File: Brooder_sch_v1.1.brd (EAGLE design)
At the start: 90 x 75 mm, 30 parts, among them J1 DCJ0202, J2 1X2-3.5MM, J3 DCJ0202, J4 1X2-3.5MM, U1 328P

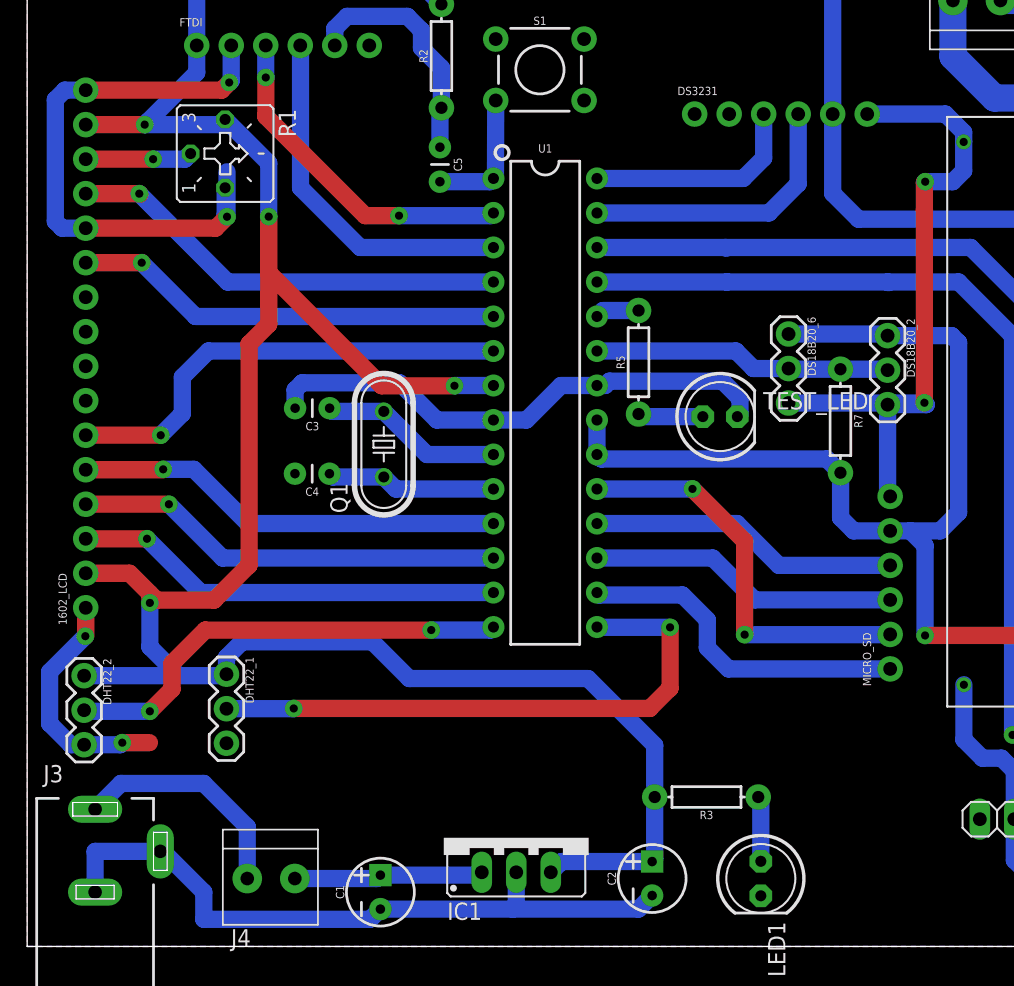
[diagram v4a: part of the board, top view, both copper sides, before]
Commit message: Links lcd and dht grounds
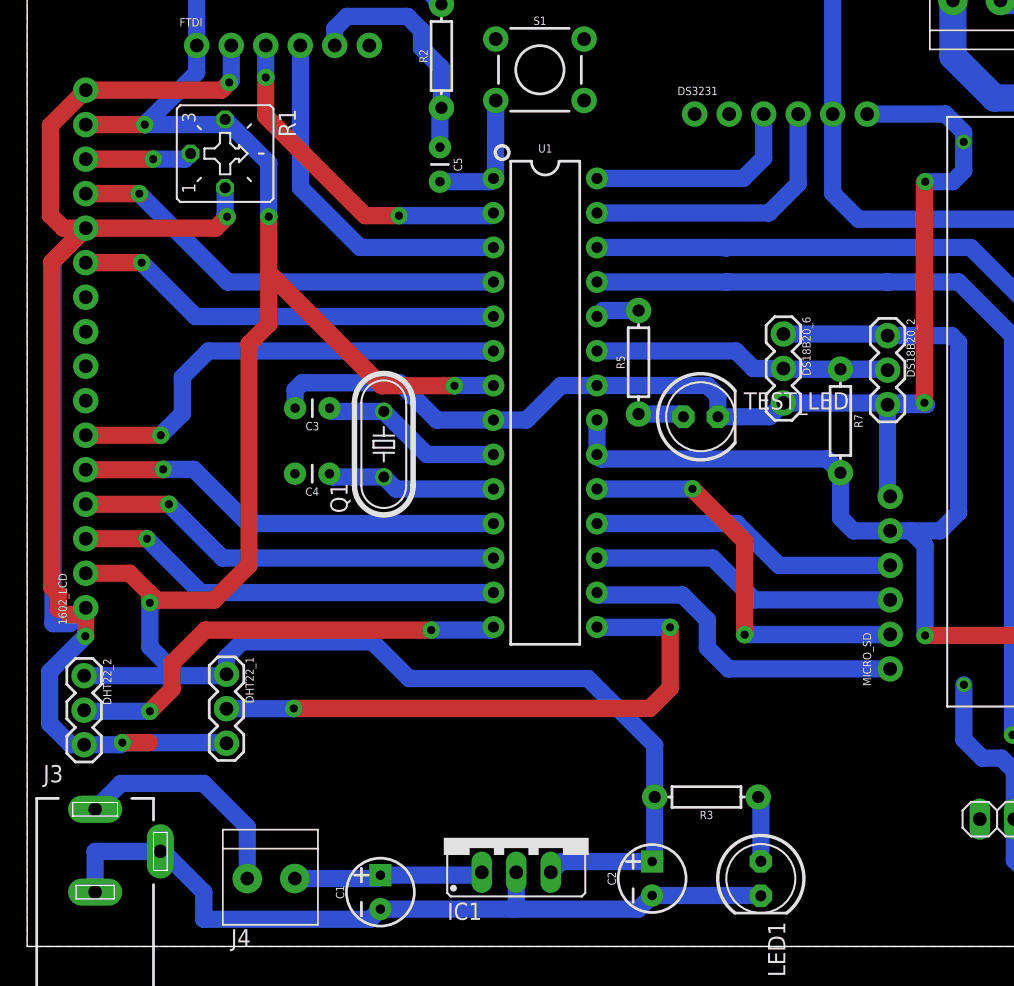
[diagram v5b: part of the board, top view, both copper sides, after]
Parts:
- moved TEST_LED 1.43 mm to (49.6, 39.0)
- moved DS18B20_6 0.38 mm to (55.7, 45.1)
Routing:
- net GND: track 236.1 -> 315.9 mm
- net N$1: track 4.81 -> 3.38 mm
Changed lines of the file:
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@@
 <attribute name="PROD_ID" value="XXX-00000" x="63.33" y="44.96" size="1.778" layer="27" rot="R270" display="off"/>
 </element>
-<element name="DS18B20_6" library="SparkFun-Connectors" package="1X03" value="455-1750-1-ND" x="56.04" y="45.08" rot="R270">
-<attribute name="PROD_ID" value="XXX-00000" x="56.04" y="45.08" size="1.778" layer="27" rot="R270" display="off"/>
+<element name="DS18B20_6" library="SparkFun-Connectors" package="1X03" value="455-1750-1-ND" x="55.66" y="45.08" rot="R270">
+<attribute name="PROD_ID" value="XXX-00000" x="55.66" y="45.08" size="1.778" layer="27" rot="R270" display="off"/>
 </element>
 <element name="FTDI" library="SparkFun-Connectors" package="1X06_NO_SILK" value="" x="12.48" y="66.32">
@@
 <attribute name="PROD_ID" value="RES-09327" x="45" y="43" size="1.778" layer="27" rot="R90" display="off"/>
 </element>
-<element name="TEST_LED" library="adafruit" package="LED5MM" value="" x="51" y="39"/>
+<element name="TEST_LED" library="adafruit" package="LED5MM" value="" x="49.57" y="38.99"/>
 <element name="DS3231" library="SparkFun-Connectors" package="1X06_NO_SILK" value="" x="49.13" y="61.27">
 <attribute name="PROD_ID" value="CONN-08437" x="49.13" y="61.27" size="1.778" layer="27" display="off"/>
@@
 <wire x1="13.87" y1="52.87" x2="14.71" y2="53.71" width="1.27" layer="1"/>
 <via x="14.71" y="53.71" extent="1-16" drill="0.6" diameter="1.3"/>
-<wire x1="14.71" y1="53.71" x2="14.71" y2="57.02" width="1.27" layer="16"/>
-<wire x1="52.47" y1="40.32" x2="52.47" y2="39.2" width="1.27" layer="16"/>
-<wire x1="52.47" y1="39.2" x2="52.27" y2="39" width="1.27" layer="16"/>
 <wire x1="41.94" y1="41.29" x2="42.54" y2="41.29" width="1.27" layer="16"/>
-<wire x1="42.54" y1="41.29" x2="42.86" y2="41.61" width="1.27" layer="16"/>
-<wire x1="42.86" y1="41.61" x2="51.18" y2="41.61" width="1.27" layer="16"/>
-<wire x1="51.18" y1="41.61" x2="52.47" y2="40.32" width="1.27" layer="16"/>
 <contactref element="U$2" pad="IN(-VE)"/>
 <contactref element="U$2" pad="OUT(-VE)"/>
@@
 <via x="66.04" y="40.02" extent="1-16" drill="0.6" diameter="1.3"/>
 <wire x1="66.04" y1="40.02" x2="66.02" y2="40" width="1.27" layer="16"/>
-<wire x1="66.02" y1="40" x2="56.04" y2="40" width="1.27" layer="16"/>
+<wire x1="66.02" y1="40" x2="55.66" y2="40" width="1.27" layer="16"/>
 <wire x1="66.04" y1="40.02" x2="66.18" y2="39.88" width="1.27" layer="16"/>
 <wire x1="66.18" y1="39.88" x2="63.33" y2="39.88" width="1.27" layer="16"/>
@@
 <wire x1="39.29" y1="41.29" x2="41.94" y2="41.29" width="1.27" layer="16"/>
 <wire x1="36.75" y1="38.75" x2="39.29" y2="41.29" width="1.27" layer="16"/>
-<wire x1="4.31" y1="52.87" x2="2.57" y2="52.87" width="1.27" layer="16"/>
-<wire x1="2.57" y1="52.87" x2="2.07" y2="53.37" width="1.27" layer="16"/>
-<wire x1="2.07" y1="53.37" x2="2.07" y2="62.33" width="1.27" layer="16"/>
-<wire x1="2.77" y1="63.03" x2="4.31" y2="63.03" width="1.27" layer="16"/>
-<wire x1="2.07" y1="62.33" x2="2.77" y2="63.03" width="1.27" layer="16"/>
 <wire x1="85.57" y1="67.95" x2="85.57" y2="69.75" width="2" layer="16"/>
 <wire x1="85.57" y1="69.75" x2="82.57" y2="72.75" width="2" layer="16"/>
@@
 <wire x1="14.57" y1="55.8454" x2="14.57" y2="53.85" width="1.27" layer="16"/>
 <wire x1="14.57" y1="53.85" x2="14.71" y2="53.71" width="1.27" layer="16"/>
+<wire x1="7" y1="15" x2="14.63" y2="15" width="1.27" layer="16"/>
+<wire x1="14.63" y1="15" x2="14.67" y2="14.96" width="1.27" layer="16"/>
+<wire x1="4.31" y1="52.87" x2="1.9" y2="50.46" width="1.27" layer="16"/>
+<wire x1="1.9" y1="50.46" x2="1.9" y2="23.76" width="1.27" layer="16"/>
+<wire x1="1.9" y1="23.76" x2="3.14" y2="23.76" width="1.27" layer="16"/>
+<wire x1="3.14" y1="23.76" x2="4.31" y2="24.93" width="1.27" layer="16"/>
+<wire x1="4.31" y1="63.03" x2="1.71" y2="60.43" width="1.27" layer="1"/>
+<wire x1="2.66" y1="52.87" x2="4.31" y2="52.87" width="1.27" layer="1"/>
+<wire x1="1.71" y1="60.43" x2="1.71" y2="53.82" width="1.27" layer="1"/>
+<wire x1="1.71" y1="53.82" x2="2.66" y2="52.87" width="1.27" layer="1"/>
+<wire x1="4.31" y1="52.87" x2="1.81" y2="50.37" width="1.27" layer="1"/>
+<wire x1="1.81" y1="50.37" x2="1.81" y2="26.43" width="1.27" layer="1"/>
+<wire x1="1.81" y1="26.43" x2="2.29" y2="25.95" width="1.27" layer="1"/>
+<wire x1="2.29" y1="25.95" x2="2.29" y2="24.81" width="1.27" layer="1"/>
+<wire x1="4.31" y1="24.93" x2="3.8" y2="24.42" width="1.27" layer="1"/>
+<wire x1="3.8" y1="24.42" x2="3.05" y2="24.42" width="1.27" layer="1"/>
+<wire x1="41.94" y1="41.29" x2="50.07" y2="41.29" width="1.27" layer="16"/>
+<wire x1="50.84" y1="40.52" x2="50.84" y2="38.99" width="1.27" layer="16"/>
+<wire x1="50.07" y1="41.29" x2="50.84" y2="40.52" width="1.27" layer="16"/>
+<wire x1="50.84" y1="38.99" x2="54.65" y2="38.99" width="1.27" layer="16"/>
+<wire x1="54.65" y1="38.99" x2="55.66" y2="40" width="1.27" layer="16"/>
+<wire x1="46" y1="3.75" x2="53.98" y2="3.75" width="1.27" layer="16"/>
+<wire x1="53.98" y1="3.75" x2="54" y2="3.73" width="1.27" layer="16"/>
+<wire x1="68.9319125" y1="59.9280875" x2="85.57" y2="67.95" width="0" layer="19" extent="16-16"/>
+<wire x1="19.71" y1="34.8" x2="19.72" y2="39.62" width="0" layer="19" extent="1-1"/>
+<wire x1="13.87" y1="52.87" x2="20.24" y2="41.49" width="0" layer="19" extent="1-16"/>
+<wire x1="5" y1="7" x2="4.19" y2="14.85" width="0" layer="19" extent="16-16"/>
+<wire x1="68.945340625" y1="19.264259375" x2="63.52" y2="33.13" width="0" layer="19" extent="1-1"/>
+<wire x1="34.4888" y1="66.7906" x2="15.02" y2="66.32" width="0" layer="19" extent="1-1"/>
 </signal>
 <signal name="12V">
@@
 <wire x1="59.87" y1="31.55" x2="60.83" y2="30.59" width="1.27" layer="16"/>
 <wire x1="60.83" y1="30.59" x2="63.52" y2="30.59" width="1.27" layer="16"/>
-<wire x1="56.04" y1="45.08" x2="63.21" y2="45.08" width="1.27" layer="16"/>
+<wire x1="55.66" y1="45.08" x2="63.21" y2="45.08" width="1.27" layer="16"/>
 <wire x1="63.21" y1="45.08" x2="63.33" y2="44.96" width="1.27" layer="16"/>
 <wire x1="80.28" y1="9.37" x2="80.28" y2="15.66" width="1.27" layer="16"/>
@@
 <contactref element="DS18B20_6" pad="2"/>
 <wire x1="41.94" y1="43.83" x2="52.17" y2="43.83" width="1.27" layer="16"/>
-<wire x1="53.46" y1="42.54" x2="56.04" y2="42.54" width="1.27" layer="16"/>
+<wire x1="53.46" y1="42.54" x2="55.66" y2="42.54" width="1.27" layer="16"/>
 <wire x1="52.17" y1="43.83" x2="53.46" y2="42.54" width="1.27" layer="16"/>
-<wire x1="56.04" y1="42.54" x2="56.09" y2="42.49" width="1.27" layer="16"/>
+<wire x1="55.66" y1="42.54" x2="56.09" y2="42.49" width="1.27" layer="16"/>
 <wire x1="56.09" y1="42.49" x2="59.86" y2="42.49" width="1.27" layer="16"/>
 <wire x1="59.86" y1="42.49" x2="63.26" y2="42.49" width="1.27" layer="16"/>
@@
 <contactref element="R5" pad="P$1"/>
 <contactref element="TEST_LED" pad="A"/>
-<wire x1="45" y1="39.19" x2="45.19" y2="39" width="1.27" layer="16"/>
-<wire x1="45.19" y1="39" x2="49.73" y2="39" width="1.27" layer="16"/>
+<wire x1="45" y1="39.19" x2="48.1" y2="39.19" width="1.27" layer="16"/>
+<wire x1="48.1" y1="39.19" x2="48.3" y2="38.99" width="1.27" layer="16"/>
 </signal>
 <signal name="PC1">

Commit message: Adds ICSP header
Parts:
- added JP1: (no value), pinhead:2X03
- moved MICRO_SD 6.27 mm to (57.2, 20.4)
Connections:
- net PB2 renamed SS
- removed net N$4: C5.2, S1.3, U1.1
- removed net PB3: MICRO_SD.3, U1.17
- removed net PB4: MICRO_SD.4, U1.18
- removed net PB5: MICRO_SD.2, U1.19
- new net MISO: JP1.1, MICRO_SD.4, U1.18
- new net MOSI: JP1.4, MICRO_SD.3, U1.17
- new net RESET: C5.2, JP1.5, S1.3, U1.1
- new net SCK: JP1.3, MICRO_SD.2, U1.19
- net 5V: now also JP1.2
- net GND: now also JP1.6
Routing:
- net RESET: track 0.00 -> 108.6 mm, vias 0 -> 2
- net GND: track 315.9 -> 387.3 mm
- net MOSI: track 0.00 -> 53.9 mm, vias 0 -> 2
- net PB5: track 30.1 -> 0.00 mm, vias 2 -> 0
- net SCK: track 0.00 -> 29.7 mm, vias 0 -> 2
- net PB4: track 22.9 -> 0.00 mm
- net PB3: track 22.9 -> 0.00 mm
- net MISO: track 0.00 -> 20.8 mm
- net N$4: track 9.84 -> 0.00 mm
- net SS: track 25.1 -> 18.6 mm
- net 5V: track 377.1 -> 382.0 mm, vias 6 -> 9

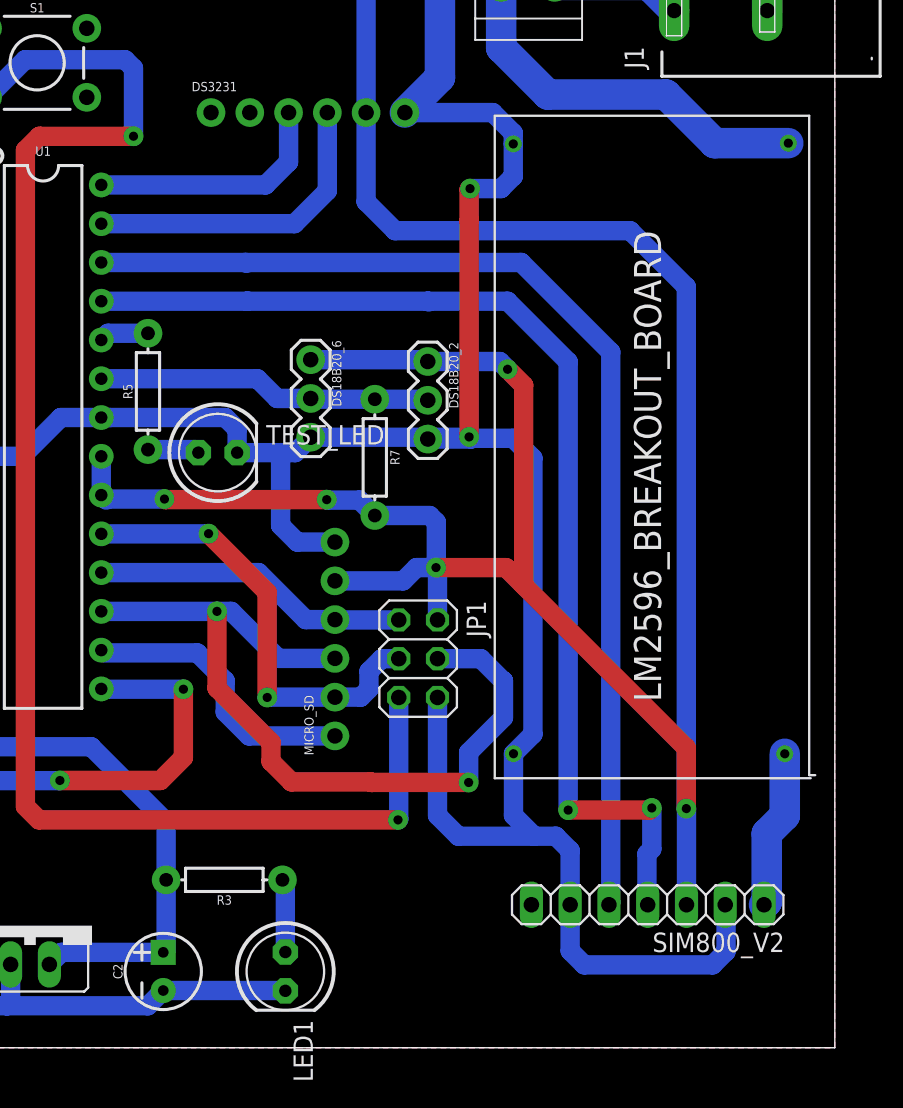
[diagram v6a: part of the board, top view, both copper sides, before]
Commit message: Switches orientation of the sim800l
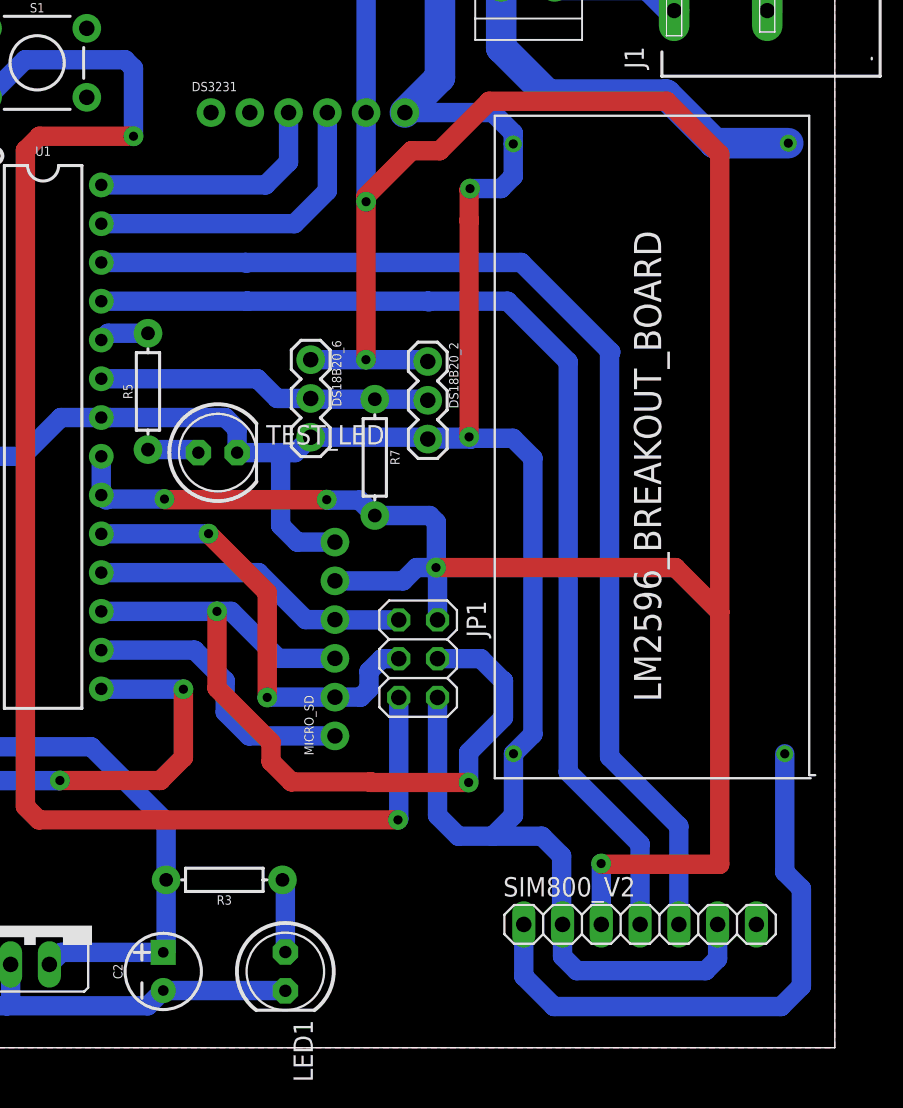
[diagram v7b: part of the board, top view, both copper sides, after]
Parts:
- moved SIM800_V2 1.38 mm to (77.2, 8.08), turned to 0 degrees
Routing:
- net 5V_SIM: track 10.5 -> 38.6 mm
- net 5V: track 382.0 -> 388.9 mm, vias 9 -> 10
- net RX: track 72.2 -> 75.3 mm
- net TX: track 73.7 -> 71.1 mm, vias 2 -> 0
- net GND: track 387.3 -> 386.0 mm
